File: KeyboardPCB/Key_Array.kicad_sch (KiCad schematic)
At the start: 138 parts

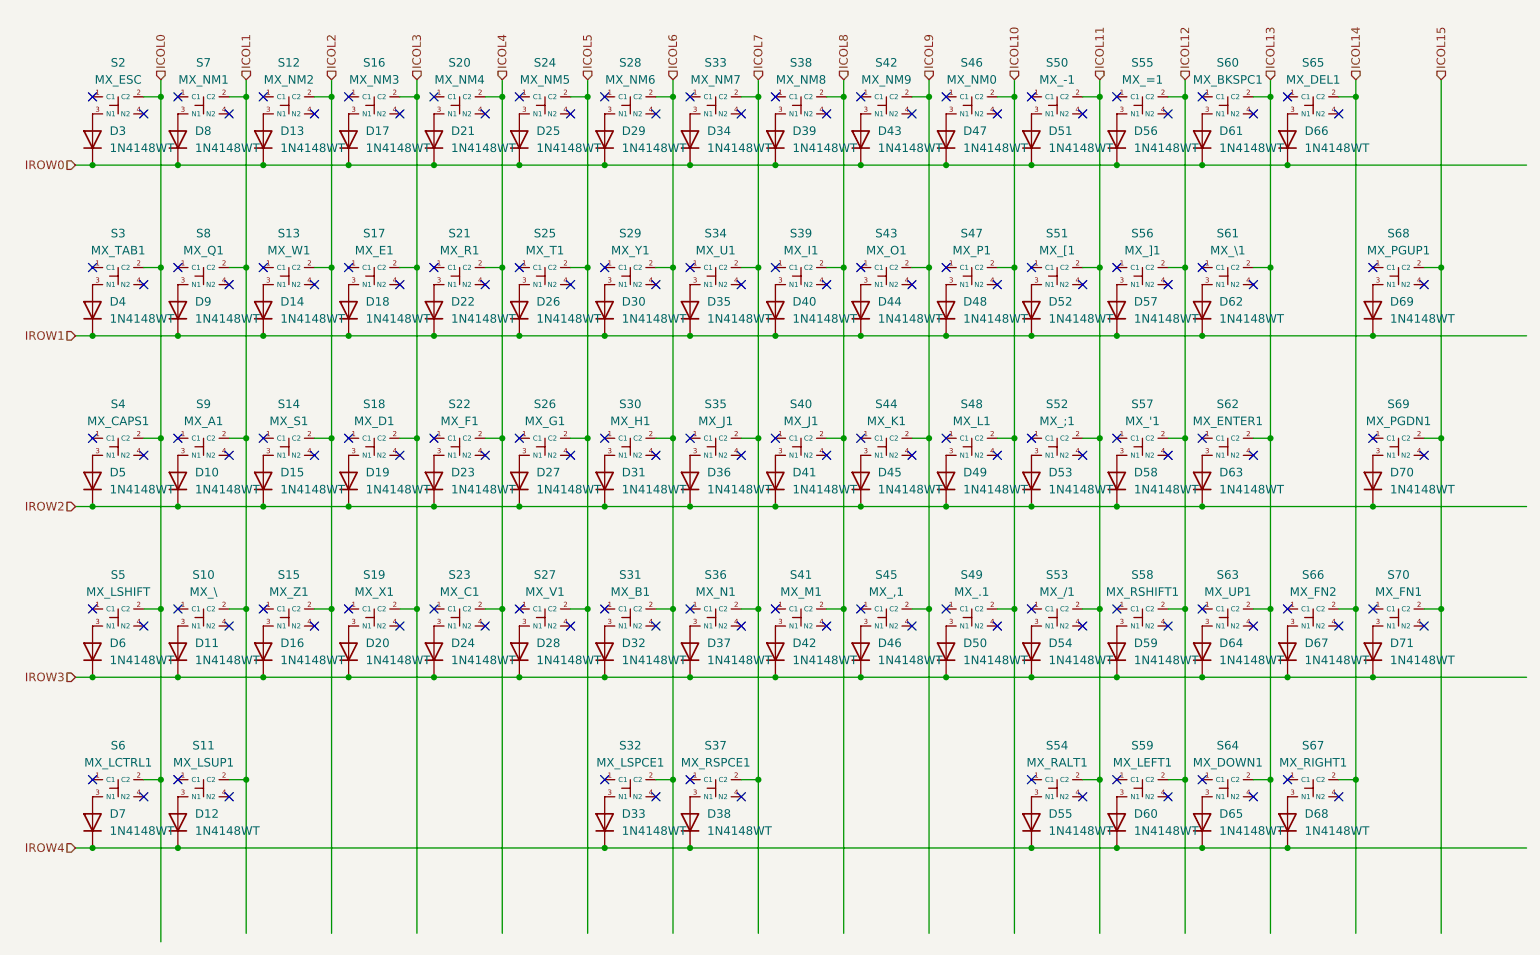
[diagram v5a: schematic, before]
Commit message: Changed switch and revised PCB layout?
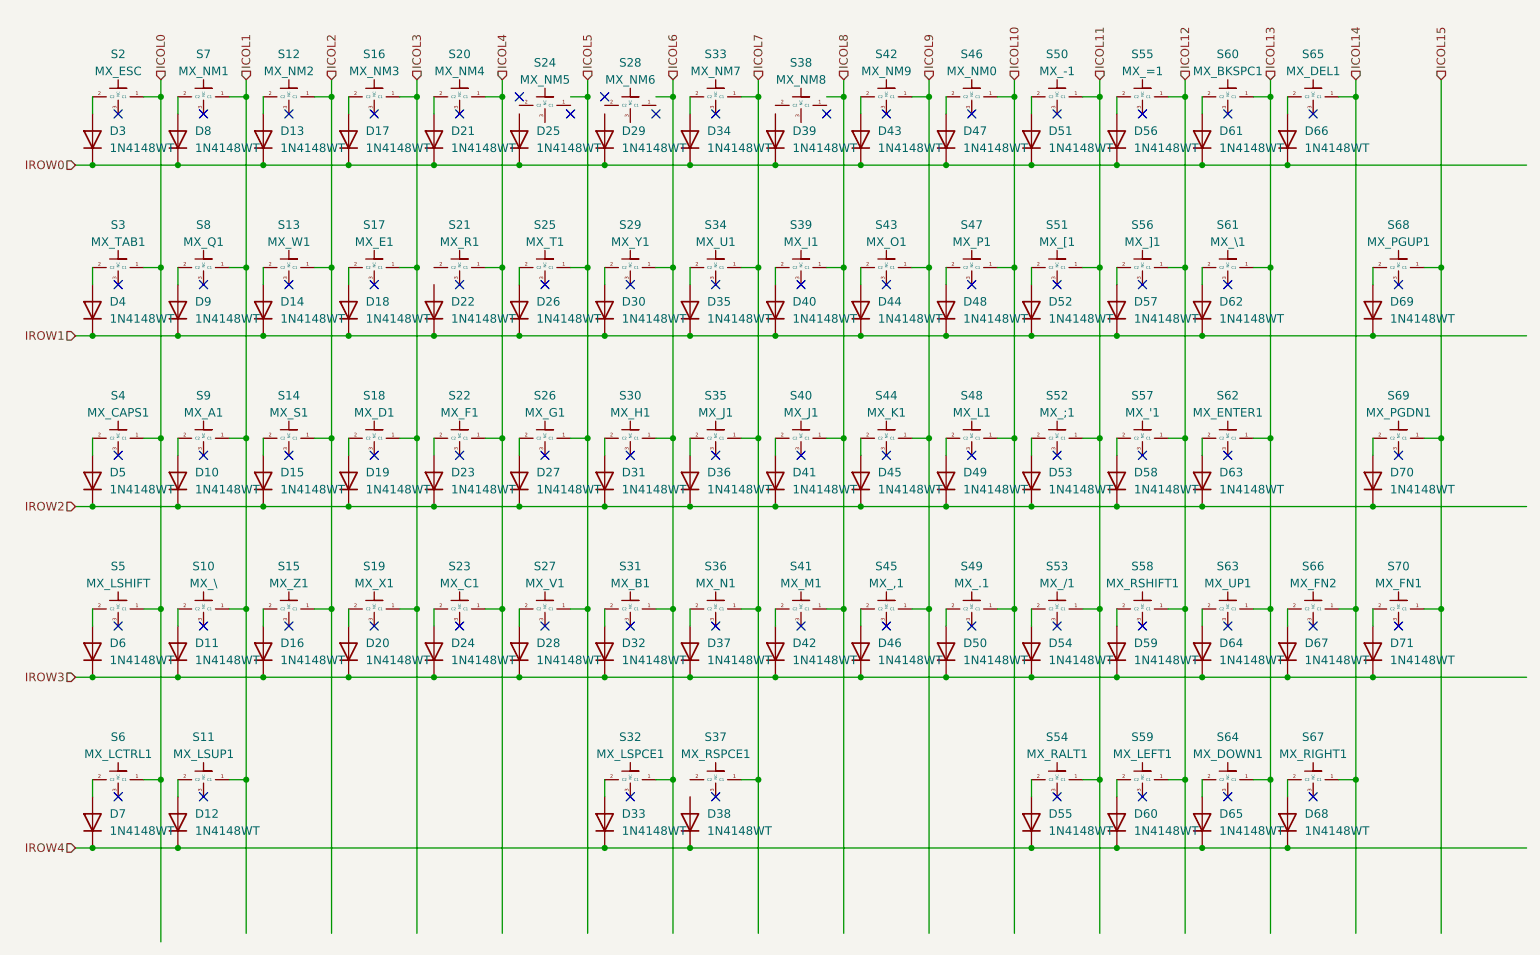
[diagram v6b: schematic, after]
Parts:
- S10, S11, S12, S13, S14, S15, S16, S17, S18, S19, S2, S20, S21, S22, S23, S24, S25, S26, S27, S28, S29, S3, S30, S31, S32, S33, S34, S35, S36, S37, S38, S39, S4, S40, S41, S42, S43, S44, S45, S46, S47, S48, S49, S5, S50, S51, S52, S53, S54, S55, S56, S57, S58, S59, S6, S60, S61, S62, S63, S64, S65, S66, S67, S68, S69, S7, S70, S8, S9: footprint keyboard_syms:B3FS1012P -> keyboard_syms:B3U1100PB; symbol keyboard_syms:B3FS-1012P -> keyboard_syms:B3U-1100P-B; Arrow Part Number B3FS-1012P -> B3U-1100P-B; Arrow Price/Stock https://www.arrow.com/en/products/b3fs-1012p/omron?region=n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 -> https://www.arrow.com/en/products/b3u-1100p-b/omron?region=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; Height 4.3 -> 1.75; Manufacturer_Part_Number B3FS-1012P -> B3U-1100P-B; Mouser Part Number 653-B3FS-1012P -> 653-B3U-1100P-B; Mouser Price/Stock https://www.mouser.co.uk/ProductDetail/Omron-Electronics/B3FS-1012P?qs=1tDaWCEHQQ7mwfTJVAKWQA%3D%3D -> https://www.mouser.co.uk/ProductDetail/Omron-Electronics/B3U-1100P-B?qs=q8ECNkb1%2FvOX21F1CoxJgQ%3D%3D
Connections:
- net ICOL0: now also S2.1 (C1), S3.1 (C1), S4.1 (C1), S5.1 (C1), S6.1 (C1); no longer S2.2 (C2), S3.2 (C2), S4.2 (C2), S5.2 (C2), S6.2 (C2)
- net ICOL1: now also S10.1 (C1), S11.1 (C1), S7.1 (C1), S8.1 (C1), S9.1 (C1); no longer S10.2 (C2), S11.2 (C2), S7.2 (C2), S8.2 (C2), S9.2 (C2)
- net ICOL10: now also S46.1 (C1), S47.1 (C1), S48.1 (C1), S49.1 (C1); no longer S46.2 (C2), S47.2 (C2), S48.2 (C2), S49.2 (C2)
- net ICOL11: now also S50.1 (C1), S51.1 (C1), S52.1 (C1), S53.1 (C1), S54.1 (C1); no longer S50.2 (C2), S51.2 (C2), S52.2 (C2), S53.2 (C2), S54.2 (C2)
- net ICOL12: now also S55.1 (C1), S56.1 (C1), S57.1 (C1), S58.1 (C1), S59.1 (C1); no longer S55.2 (C2), S56.2 (C2), S57.2 (C2), S58.2 (C2), S59.2 (C2)
- net ICOL13: now also S60.1 (C1), S61.1 (C1), S62.1 (C1), S63.1 (C1), S64.1 (C1); no longer S60.2 (C2), S61.2 (C2), S62.2 (C2), S63.2 (C2), S64.2 (C2)
- net ICOL14: now also S65.1 (C1), S66.1 (C1), S67.1 (C1); no longer S65.2 (C2), S66.2 (C2), S67.2 (C2)
- net ICOL15: now also S68.1 (C1), S69.1 (C1), S70.1 (C1); no longer S68.2 (C2), S69.2 (C2), S70.2 (C2)
- net ICOL2: now also S12.1 (C1), S13.1 (C1), S14.1 (C1), S15.1 (C1); no longer S12.2 (C2), S13.2 (C2), S14.2 (C2), S15.2 (C2)
- net ICOL3: now also S16.1 (C1), S17.1 (C1), S18.1 (C1), S19.1 (C1); no longer S16.2 (C2), S17.2 (C2), S18.2 (C2), S19.2 (C2)
- net ICOL4: now also S20.1 (C1), S21.1 (C1), S22.1 (C1), S23.1 (C1); no longer S20.2 (C2), S21.2 (C2), S22.2 (C2), S23.2 (C2)
- net ICOL5: now also S25.1 (C1), S26.1 (C1), S27.1 (C1); no longer S24.2 (C2), S25.2 (C2), S26.2 (C2), S27.2 (C2)
- net ICOL6: now also S29.1 (C1), S30.1 (C1), S31.1 (C1), S32.1 (C1); no longer S28.2 (C2), S29.2 (C2), S30.2 (C2), S31.2 (C2), S32.2 (C2)
- net ICOL7: now also S33.1 (C1), S34.1 (C1), S35.1 (C1), S36.1 (C1), S37.1 (C1); no longer S33.2 (C2), S34.2 (C2), S35.2 (C2), S36.2 (C2), S37.2 (C2)
- net ICOL8: now also S39.1 (C1), S40.1 (C1), S41.1 (C1); no longer S38.2 (C2), S39.2 (C2), S40.2 (C2), S41.2 (C2)
- net ICOL9: now also S42.1 (C1), S43.1 (C1), S44.1 (C1), S45.1 (C1); no longer S42.2 (C2), S43.2 (C2), S44.2 (C2), S45.2 (C2)
- net at D34.2 (A): now also S33.2 (C2); no longer S33.3 (N1)
- net at D59.2 (A): now also S58.2 (C2); no longer S58.3 (N1)
- net at D22.2 (A): no longer S21.3 (N1)
- net at D18.2 (A): now also S17.2 (C2); no longer S17.3 (N1)
- net at D25.2 (A): no longer S24.3 (N1)
- net at D71.2 (A): now also S70.2 (C2); no longer S70.3 (N1)
- net at D49.2 (A): now also S48.2 (C2); no longer S48.3 (N1)
- net at D61.2 (A): now also S60.2 (C2); no longer S60.3 (N1)
- net at D54.2 (A): now also S53.2 (C2); no longer S53.3 (N1)
- net at D60.2 (A): now also S59.2 (C2); no longer S59.3 (N1)
- net at D13.2 (A): now also S12.2 (C2); no longer S12.3 (N1)
- net at D30.2 (A): now also S29.2 (C2); no longer S29.3 (N1)
- net at D38.2 (A): no longer S37.3 (N1)
- net at S38.3 (NC): no longer D39.2 (A)
- net at D43.2 (A): now also S42.2 (C2); no longer S42.3 (N1)
- net at D20.2 (A): now also S19.2 (C2); no longer S19.3 (N1)
- net at D27.2 (A): now also S26.2 (C2); no longer S26.3 (N1)
- net at D63.2 (A): now also S62.2 (C2); no longer S62.3 (N1)
- net at D26.2 (A): now also S25.2 (C2); no longer S25.3 (N1)
- net at D62.2 (A): now also S61.2 (C2); no longer S61.3 (N1)
- net at D55.2 (A): now also S54.2 (C2); no longer S54.3 (N1)
- net at D50.2 (A): now also S49.2 (C2); no longer S49.3 (N1)
- net at D64.2 (A): now also S63.2 (C2); no longer S63.3 (N1)
- net at D33.2 (A): now also S32.2 (C2); no longer S32.3 (N1)
- net at D12.2 (A): now also S11.2 (C2); no longer S11.3 (N1)
- net at D58.2 (A): now also S57.2 (C2); no longer S57.3 (N1)
- net at D68.2 (A): now also S67.2 (C2); no longer S67.3 (N1)
- net at D67.2 (A): now also S66.2 (C2); no longer S66.3 (N1)
- net at D66.2 (A): now also S65.2 (C2); no longer S65.3 (N1)
- net at D23.2 (A): now also S22.2 (C2); no longer S22.3 (N1)
- net at D5.2 (A): now also S4.2 (C2); no longer S4.3 (N1)
- net at D52.2 (A): now also S51.2 (C2); no longer S51.3 (N1)
- net at D19.2 (A): now also S18.2 (C2); no longer S18.3 (N1)
- net at D3.2 (A): now also S2.2 (C2); no longer S2.3 (N1)
- net at D40.2 (A): now also S39.2 (C2); no longer S39.3 (N1)
- net at D57.2 (A): now also S56.2 (C2); no longer S56.3 (N1)
- net at D24.2 (A): now also S23.2 (C2); no longer S23.3 (N1)
- net at D28.2 (A): now also S27.2 (C2); no longer S27.3 (N1)
- net at D31.2 (A): now also S30.2 (C2); no longer S30.3 (N1)
- net at D70.2 (A): now also S69.2 (C2); no longer S69.3 (N1)
- net at S28.3 (NC): no longer D29.2 (A)
- net at D17.2 (A): now also S16.2 (C2); no longer S16.3 (N1)
- net at D51.2 (A): now also S50.2 (C2); no longer S50.3 (N1)
- net at D42.2 (A): now also S41.2 (C2); no longer S41.3 (N1)
- net at D14.2 (A): now also S13.2 (C2); no longer S13.3 (N1)
- net at D53.2 (A): now also S52.2 (C2); no longer S52.3 (N1)
- net at D47.2 (A): now also S46.2 (C2); no longer S46.3 (N1)
- net at D36.2 (A): now also S35.2 (C2); no longer S35.3 (N1)
- net at D9.2 (A): now also S8.2 (C2); no longer S8.3 (N1)
- net at D69.2 (A): now also S68.2 (C2); no longer S68.3 (N1)
- net at D7.2 (A): now also S6.2 (C2); no longer S6.3 (N1)
- net at D44.2 (A): now also S43.2 (C2); no longer S43.3 (N1)
- net at D21.2 (A): now also S20.2 (C2); no longer S20.3 (N1)
- net at D32.2 (A): now also S31.2 (C2); no longer S31.3 (N1)
- net at D46.2 (A): now also S45.2 (C2); no longer S45.3 (N1)
- net at D6.2 (A): now also S5.2 (C2); no longer S5.3 (N1)
- net at D48.2 (A): now also S47.2 (C2); no longer S47.3 (N1)
- net at D15.2 (A): now also S14.2 (C2); no longer S14.3 (N1)
- net at D37.2 (A): now also S36.2 (C2); no longer S36.3 (N1)
- net at D10.2 (A): now also S9.2 (C2); no longer S9.3 (N1)
- net at D8.2 (A): now also S7.2 (C2); no longer S7.3 (N1)
- net at D35.2 (A): now also S34.2 (C2); no longer S34.3 (N1)
- net at D41.2 (A): now also S40.2 (C2); no longer S40.3 (N1)
- net at D4.2 (A): now also S3.2 (C2); no longer S3.3 (N1)
- net at D65.2 (A): now also S64.2 (C2); no longer S64.3 (N1)
- net at D16.2 (A): now also S15.2 (C2); no longer S15.3 (N1)
- net at D45.2 (A): now also S44.2 (C2); no longer S44.3 (N1)
- net at D11.2 (A): now also S10.2 (C2); no longer S10.3 (N1)
- net at D56.2 (A): now also S55.2 (C2); no longer S55.3 (N1)
- no-connect marks 138 -> 71

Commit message: Finalised schematic, progress on board layout
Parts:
- removed D55, D59: 1N4148WT, Diode_SMD:D_SOD-523, symbol Diode:1N4148WT
- removed S54: MX_RALT1, keyboard_syms:B3U1100PB, symbol keyboard_syms:B3U-1100P-B
- removed S58: MX_RSHIFT1, keyboard_syms:B3U1100PB, symbol keyboard_syms:B3U-1100P-B
- S16: renamed from S66; value MX_FN2 -> MX_FN1
- S21: renamed from S70; value MX_FN1 -> MX_FN2
- S44: renamed from S40; value MX_J1 -> MX_K1
- S49: renamed from S44; value MX_K1 -> MX_L1
- S54: renamed from S48; value MX_L1 -> MX_;1
- S59: renamed from S52; value MX_;1 -> MX_'1
- S64: renamed from S57; value MX_'1 -> MX_RSUP1
- renumbered D3 to D1, D12 to D10, D13 to D11, D14 to D12, D15 to D13, D16 to D14, D67 to D15, D17 to D16, D18 to D17, D19 to D18, D20 to D19, D4 to D2, D71 to D20, D69 to D25, D25 to D26, D26 to D27, D27 to D28, D28 to D29, D5 to D3, D70 to D30, D29 to D31, D30 to D32, D31 to D33, D32 to D34, D33 to D35, D34 to D36, D35 to D37, D36 to D38, D37 to D39, D6 to D4, D38 to D40, D39 to D41, D40 to D42, D41 to D43, D42 to D44, D60 to D45, D43 to D46, D44 to D47, D45 to D48, D46 to D49, D7 to D5, D65 to D50, D47 to D51, D48 to D52, D49 to D53, D50 to D54, D64 to D55, D51 to D56, D52 to D57, D53 to D58, D54 to D59, D8 to D6, D68 to D60, D56 to D61, D57 to D62, D58 to D63, D62 to D64, D63 to D65, D61 to D66, D66 to D67, D9 to D7, D10 to D8, D11 to D9, S16 to S17, S17 to S18, S18 to S19, S19 to S20, S20 to S22, S21 to S23, S22 to S24, S23 to S25, S68 to S26, S24 to S27, S25 to S28, S26 to S29, S27 to S30, S69 to S31, S28 to S32, S29 to S33, S30 to S34, S31 to S35, S32 to S36, S33 to S37, S34 to S38, S35 to S39, S36 to S40, S37 to S41, S38 to S42, S39 to S43, S41 to S45, S59 to S46, S42 to S47, S43 to S48, S45 to S50, S64 to S51, S46 to S52, S47 to S53, S49 to S55, S63 to S56, S50 to S57, S51 to S58, S53 to S60, S67 to S61, S55 to S62, S56 to S63, S61 to S65, S62 to S66, S60 to S67, S65 to S68
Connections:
- net ICOL10: now also S56.1 (C1)
- net ICOL11: now also S61.1 (C1)
- net ICOL12: now also S65.1 (C1), S66.1 (C1); no longer S46.1 (C1)
- net ICOL13: now also S68.1 (C1); no longer S51.1 (C1), S56.1 (C1), S65.1 (C1), S66.1 (C1)
- net ICOL14: no longer S16.1 (C1), S61.1 (C1), S68.1 (C1)
- net ICOL15: no longer S21.1 (C1), S26.1 (C1), S31.1 (C1)
- net ICOL2: now also S16.1 (C1)
- net ICOL3: now also S21.1 (C1)
- net ICOL4: now also S26.1 (C1)
- net ICOL5: now also S27.1 (C1), S31.1 (C1)
- net ICOL6: now also S32.1 (C1)
- net ICOL8: now also S42.1 (C1), S46.1 (C1)
- net ICOL9: now also S51.1 (C1)
- net IROW0: no longer D67.1 (K)
- net IROW1: now also D67.1 (K); no longer D25.1 (K), D64.1 (K)
- net IROW2: no longer D30.1 (K), D65.1 (K)
- net IROW3: now also D64.1 (K); no longer D15.1 (K), D20.1 (K), D55.1 (K)
- net IROW4: now also D15.1 (K), D20.1 (K), D25.1 (K), D30.1 (K), D55.1 (K), D65.1 (K)
- net at D22.2 (A): now also S23.2 (C2)
- net at D26.2 (A): now also S27.2 (C2)
- net at D40.2 (A): now also S41.2 (C2)
- net at S42.2 (C2): now also D41.2 (A)
- net at S32.2 (C2): now also D31.2 (A)
- no-connect marks 71 -> 67
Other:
- moved on the sheet: D15, D20, D25, D30, D45, D50, D55, D60, D64, D65, D67, S16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
